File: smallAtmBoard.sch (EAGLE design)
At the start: 25 parts, among them IC1 ATMEGA-328P, IC2 7805-V, Y1 16MHz

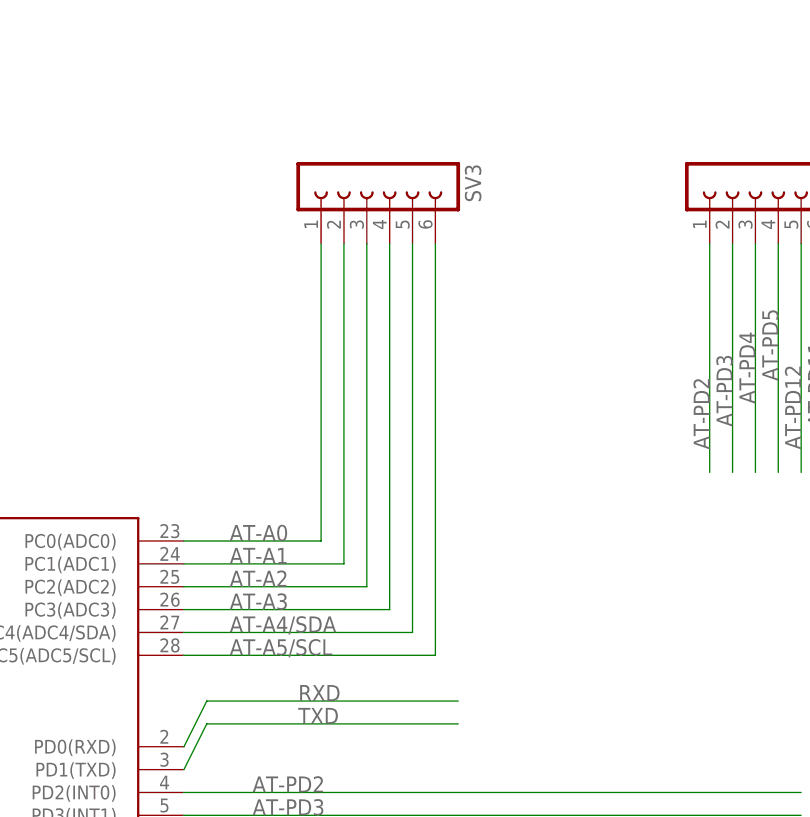
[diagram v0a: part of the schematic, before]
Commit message: smaller header
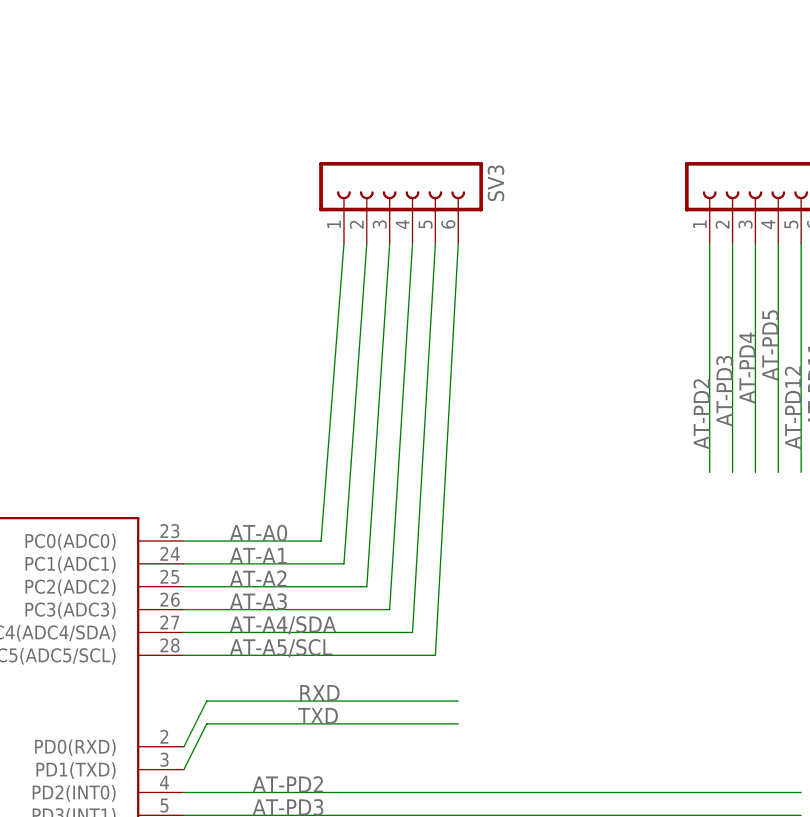
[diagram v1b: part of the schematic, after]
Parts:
- SV2: device bauteile_jbt:FE08-1 -> bauteile_jbt:FE08-1FE08-RAW
- SV3: device con-lsta:FE06-1 -> bauteile_jbt:FE06-1FE06-1-RAW
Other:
- moved on the sheet: SV3
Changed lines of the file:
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@@
 <part name="R22" library="bauteile_jbt" deviceset="R-EU_" device="0207/2V" value="2.2k"/>
 <part name="R23" library="bauteile_jbt" deviceset="R-EU_" device="0207/2V" value="2.2k"/>
-<part name="SV3" library="con-lsta" deviceset="FE06-1" device=""/>
+<part name="SV3" library="bauteile_jbt" deviceset="FE06-1" device="FE06-1-RAW"/>
 <part name="CON6" library="bauteile_jbt" deviceset="FE03-2" device=""/>
 <part name="P+3" library="supply1" deviceset="VCC" device=""/>
@@
 <part name="PAD5" library="bauteile_jbt" deviceset="PAD1,6/0,8" device="" value="D1"/>
 <part name="PAD6" library="bauteile_jbt" deviceset="PAD1,6/0,8" device="" value="D1"/>
-<part name="SV2" library="bauteile_jbt" deviceset="FE08-1" device=""/>
+<part name="SV2" library="bauteile_jbt" deviceset="FE08-1" device="FE08-RAW"/>
 <part name="U$2" library="bauteile_jbt" deviceset="FE02-2" device=""/>
 <part name="P+1" library="supply1" deviceset="VCC" device=""/>
@@
 <label x="124.46" y="91.44" size="1.778" layer="95"/>
 <pinref part="SV3" gate="G$1" pin="5"/>
-<wire x1="144.78" y1="134.62" x2="144.78" y2="91.44" width="0.1524" layer="91"/>
+<wire x1="147.32" y1="134.62" x2="144.78" y2="91.44" width="0.1524" layer="91"/>
 </segment>
 <segment>
@@
 <label x="124.46" y="93.98" size="1.778" layer="95"/>
 <pinref part="SV3" gate="G$1" pin="4"/>
-<wire x1="142.24" y1="134.62" x2="142.24" y2="93.98" width="0.1524" layer="91"/>
+<wire x1="144.78" y1="134.62" x2="142.24" y2="93.98" width="0.1524" layer="91"/>
 </segment>
 </net>
@@
 <label x="124.46" y="88.9" size="1.778" layer="95"/>
 <pinref part="SV3" gate="G$1" pin="6"/>
-<wire x1="147.32" y1="134.62" x2="147.32" y2="88.9" width="0.1524" layer="91"/>
+<wire x1="149.86" y1="134.62" x2="147.32" y2="88.9" width="0.1524" layer="91"/>
 </segment>
 <segment>
@@
 <label x="124.46" y="96.52" size="1.778" layer="95"/>
 <pinref part="SV3" gate="G$1" pin="3"/>
-<wire x1="139.7" y1="134.62" x2="139.7" y2="96.52" width="0.1524" layer="91"/>
+<wire x1="142.24" y1="134.62" x2="139.7" y2="96.52" width="0.1524" layer="91"/>
 </segment>
 </net>
@@
 <label x="124.46" y="99.06" size="1.778" layer="95"/>
 <pinref part="SV3" gate="G$1" pin="2"/>
-<wire x1="137.16" y1="134.62" x2="137.16" y2="99.06" width="0.1524" layer="91"/>
+<wire x1="139.7" y1="134.62" x2="137.16" y2="99.06" width="0.1524" layer="91"/>
 </segment>
 </net>
@@
 <label x="124.46" y="101.6" size="1.778" layer="95"/>
 <pinref part="SV3" gate="G$1" pin="1"/>
-<wire x1="134.62" y1="134.62" x2="134.62" y2="101.6" width="0.1524" layer="91"/>
-</segment>
-<segment>
+<wire x1="137.16" y1="134.62" x2="134.62" y2="101.6" width="0.1524" layer="91"/>
+</segment>
+<segment>

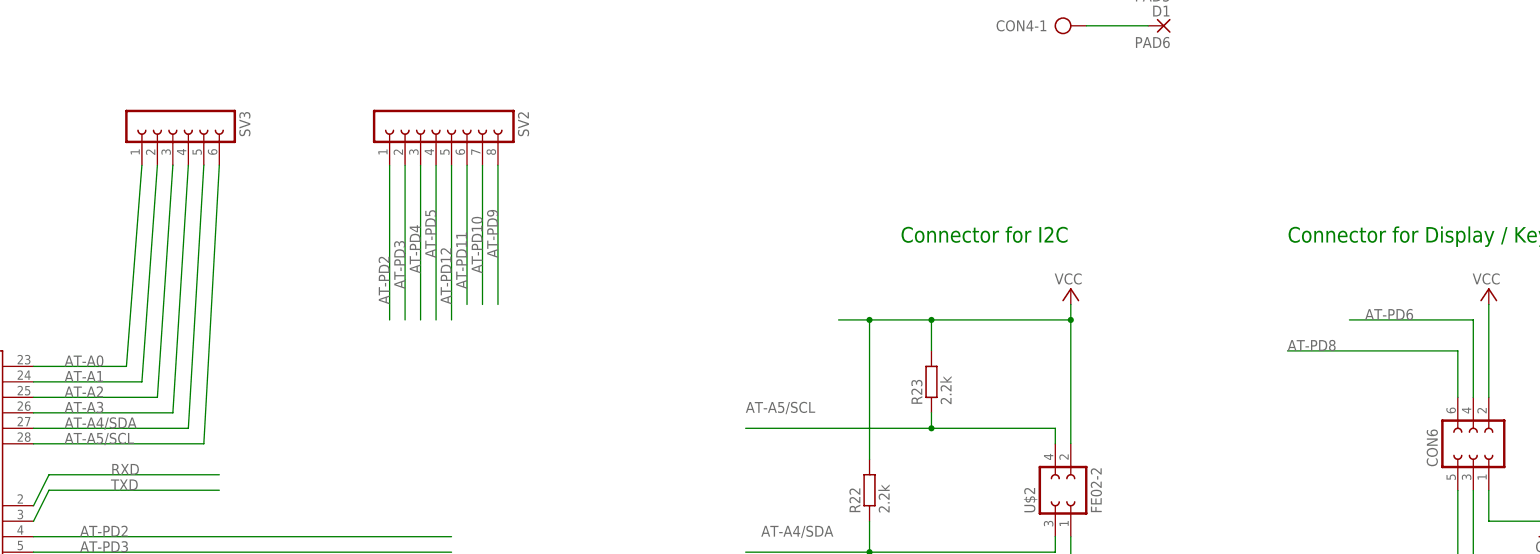
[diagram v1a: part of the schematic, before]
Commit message: standartize pins on LCD connector
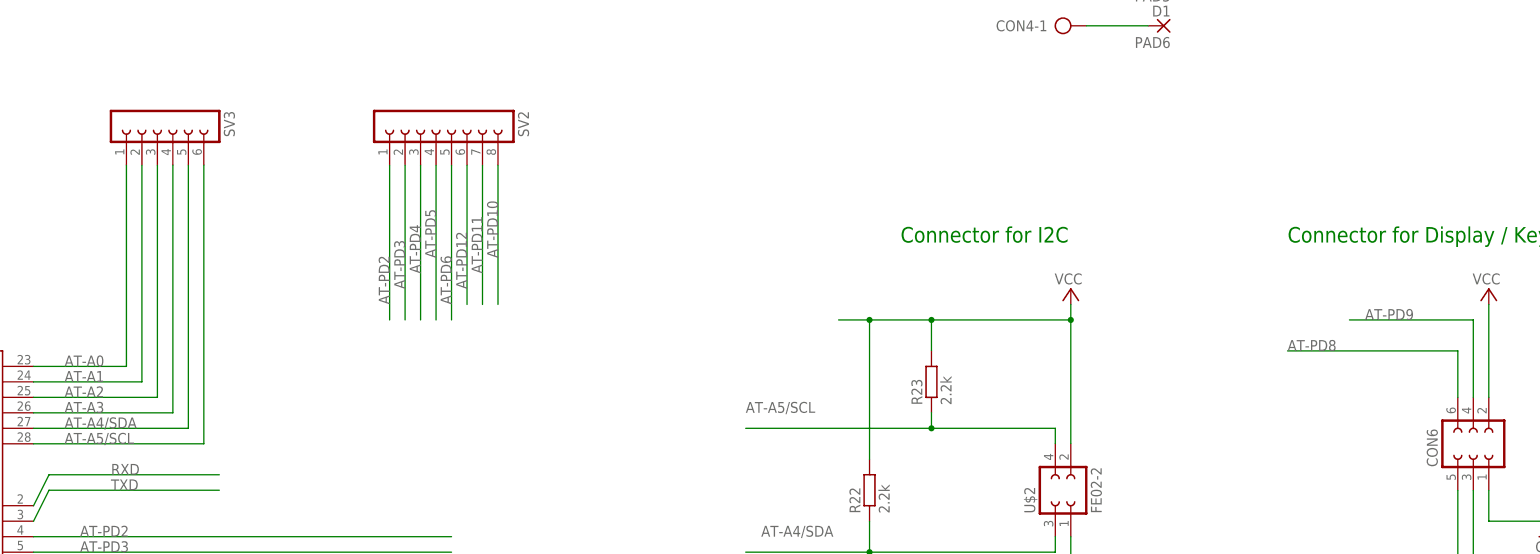
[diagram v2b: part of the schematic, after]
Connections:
- net AT-PD10: now also SV2.8; no longer SV2.7
- net AT-PD11: now also SV2.7; no longer SV2.6
- net AT-PD12: now also SV2.6; no longer SV2.5
- net AT-PD6: now also SV2.5; no longer CON6.4
- net AT-PD9: now also CON6.4; no longer SV2.8
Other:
- moved on the sheet: SV3
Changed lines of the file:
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@@
 <instance part="R22" gate="G$1" x="256.54" y="81.28" rot="R90"/>
 <instance part="R23" gate="G$1" x="266.7" y="99.06" rot="R90"/>
-<instance part="SV3" gate="G$1" x="139.7" y="142.24" rot="R270"/>
+<instance part="SV3" gate="G$1" x="137.16" y="142.24" rot="R270"/>
 <instance part="CON6" gate="G$1" x="355.6" y="88.9" rot="R90"/>
 <instance part="P+3" gate="VCC" x="358.14" y="114.3" smashed="yes">
@@
 </segment>
 <segment>
-<pinref part="CON6" gate="G$1" pin="4"/>
-<wire x1="355.6" y1="96.52" x2="355.6" y2="109.22" width="0.1524" layer="91"/>
-<wire x1="355.6" y1="109.22" x2="335.28" y2="109.22" width="0.1524" layer="91"/>
-<label x="337.82" y="109.22" size="1.778" layer="95"/>
+<pinref part="SV2" gate="G$1" pin="5"/>
+<wire x1="187.96" y1="134.62" x2="187.96" y2="109.22" width="0.1524" layer="91"/>
+<label x="187.96" y="111.76" size="1.778" layer="95" rot="R90"/>
 </segment>
 </net>
@@
 <label x="124.46" y="91.44" size="1.778" layer="95"/>
 <pinref part="SV3" gate="G$1" pin="5"/>
-<wire x1="147.32" y1="134.62" x2="144.78" y2="91.44" width="0.1524" layer="91"/>
+<wire x1="144.78" y1="134.62" x2="144.78" y2="91.44" width="0.1524" layer="91"/>
 </segment>
 <segment>
@@
 <label x="124.46" y="93.98" size="1.778" layer="95"/>
 <pinref part="SV3" gate="G$1" pin="4"/>
-<wire x1="144.78" y1="134.62" x2="142.24" y2="93.98" width="0.1524" layer="91"/>
+<wire x1="142.24" y1="134.62" x2="142.24" y2="93.98" width="0.1524" layer="91"/>
 </segment>
 </net>
@@
 </segment>
 <segment>
-<pinref part="SV2" gate="G$1" pin="7"/>
-<wire x1="193.04" y1="134.62" x2="193.04" y2="111.76" width="0.1524" layer="91"/>
-<label x="193.04" y="116.84" size="1.778" layer="95" rot="R90"/>
+<pinref part="SV2" gate="G$1" pin="8"/>
+<wire x1="195.58" y1="134.62" x2="195.58" y2="111.76" width="0.1524" layer="91"/>
+<label x="195.58" y="119.38" size="1.778" layer="95" rot="R90"/>
 </segment>
 </net>
@@
 </segment>
 <segment>
-<pinref part="SV2" gate="G$1" pin="8"/>
-<wire x1="195.58" y1="134.62" x2="195.58" y2="111.76" width="0.1524" layer="91"/>
-<label x="195.58" y="119.38" size="1.778" layer="95" rot="R90"/>
+<pinref part="CON6" gate="G$1" pin="4"/>
+<wire x1="355.6" y1="96.52" x2="355.6" y2="109.22" width="0.1524" layer="91"/>
+<wire x1="355.6" y1="109.22" x2="335.28" y2="109.22" width="0.1524" layer="91"/>
+<label x="337.82" y="109.22" size="1.778" layer="95"/>
 </segment>
 </net>
@@
 </segment>
 <segment>
-<pinref part="SV2" gate="G$1" pin="5"/>
-<wire x1="187.96" y1="134.62" x2="187.96" y2="109.22" width="0.1524" layer="91"/>
-<label x="187.96" y="111.76" size="1.778" layer="95" rot="R90"/>
+<pinref part="SV2" gate="G$1" pin="6"/>
+<wire x1="190.5" y1="134.62" x2="190.5" y2="111.76" width="0.1524" layer="91"/>
+<label x="190.5" y="114.3" size="1.778" layer="95" rot="R90"/>
 </segment>
 </net>
@@
 </segment>
 <segment>
-<pinref part="SV2" gate="G$1" pin="6"/>
-<wire x1="190.5" y1="134.62" x2="190.5" y2="111.76" width="0.1524" layer="91"/>
-<label x="190.5" y="114.3" size="1.778" layer="95" rot="R90"/>
+<pinref part="SV2" gate="G$1" pin="7"/>
+<wire x1="193.04" y1="134.62" x2="193.04" y2="111.76" width="0.1524" layer="91"/>
+<label x="193.04" y="116.84" size="1.778" layer="95" rot="R90"/>
 </segment>
 </net>
@@
 <label x="124.46" y="88.9" size="1.778" layer="95"/>
 <pinref part="SV3" gate="G$1" pin="6"/>
-<wire x1="149.86" y1="134.62" x2="147.32" y2="88.9" width="0.1524" layer="91"/>
+<wire x1="147.32" y1="134.62" x2="147.32" y2="88.9" width="0.1524" layer="91"/>
 </segment>
 <segment>
@@
 <label x="124.46" y="96.52" size="1.778" layer="95"/>
 <pinref part="SV3" gate="G$1" pin="3"/>
-<wire x1="142.24" y1="134.62" x2="139.7" y2="96.52" width="0.1524" layer="91"/>
+<wire x1="139.7" y1="134.62" x2="139.7" y2="96.52" width="0.1524" layer="91"/>
 </segment>
 </net>
@@
 <label x="124.46" y="99.06" size="1.778" layer="95"/>
 <pinref part="SV3" gate="G$1" pin="2"/>
-<wire x1="139.7" y1="134.62" x2="137.16" y2="99.06" width="0.1524" layer="91"/>
+<wire x1="137.16" y1="134.62" x2="137.16" y2="99.06" width="0.1524" layer="91"/>
 </segment>
 </net>
@@
 <label x="124.46" y="101.6" size="1.778" layer="95"/>
 <pinref part="SV3" gate="G$1" pin="1"/>
-<wire x1="137.16" y1="134.62" x2="134.62" y2="101.6" width="0.1524" layer="91"/>
-</segment>
-<segment>
+<wire x1="134.62" y1="134.62" x2="134.62" y2="101.6" width="0.1524" layer="91"/>
+</segment>
+<segment>
